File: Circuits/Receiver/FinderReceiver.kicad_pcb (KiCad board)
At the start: 2 copper layers, 59 x 28 mm, 9 parts, among them P1 WRITER-VCC, SW1 SW_PUSH, U1 TWE_LITE_SMD, U2 NJU72501MJE

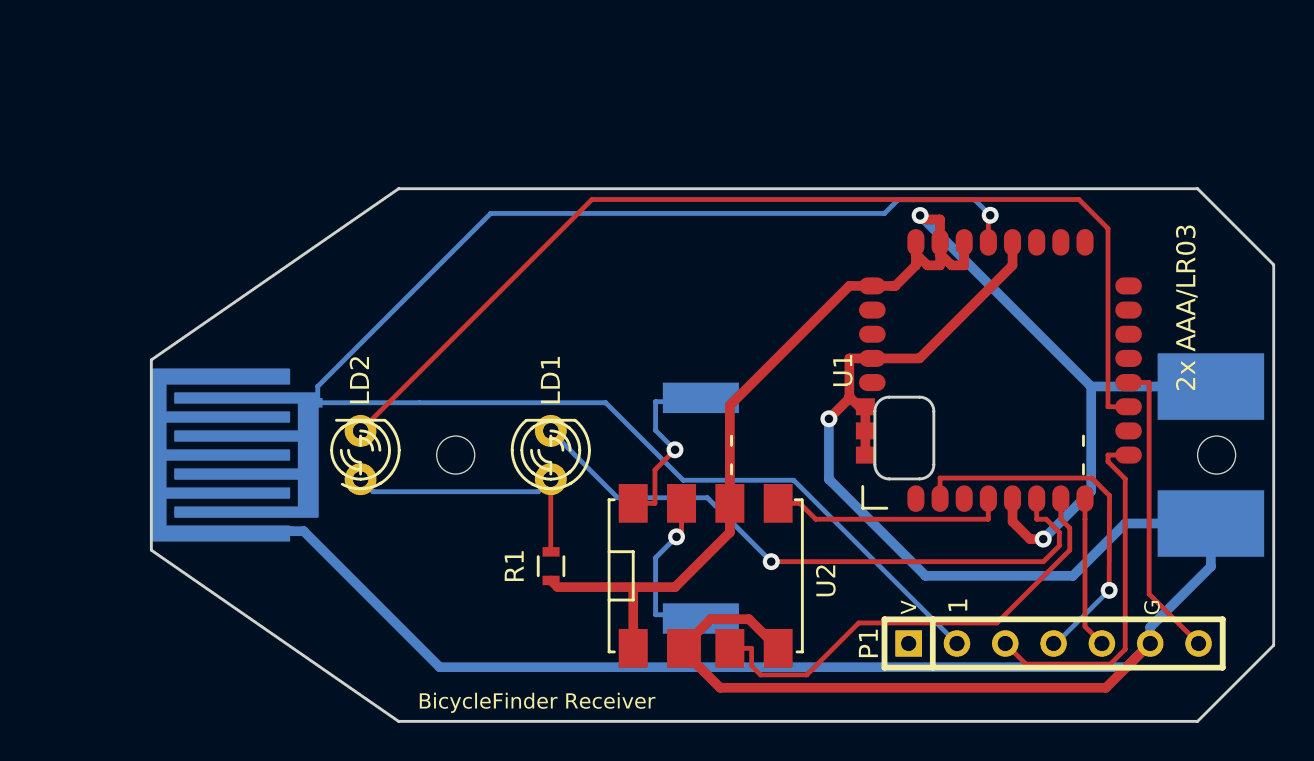
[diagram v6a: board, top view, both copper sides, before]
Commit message: Relocated all parts.
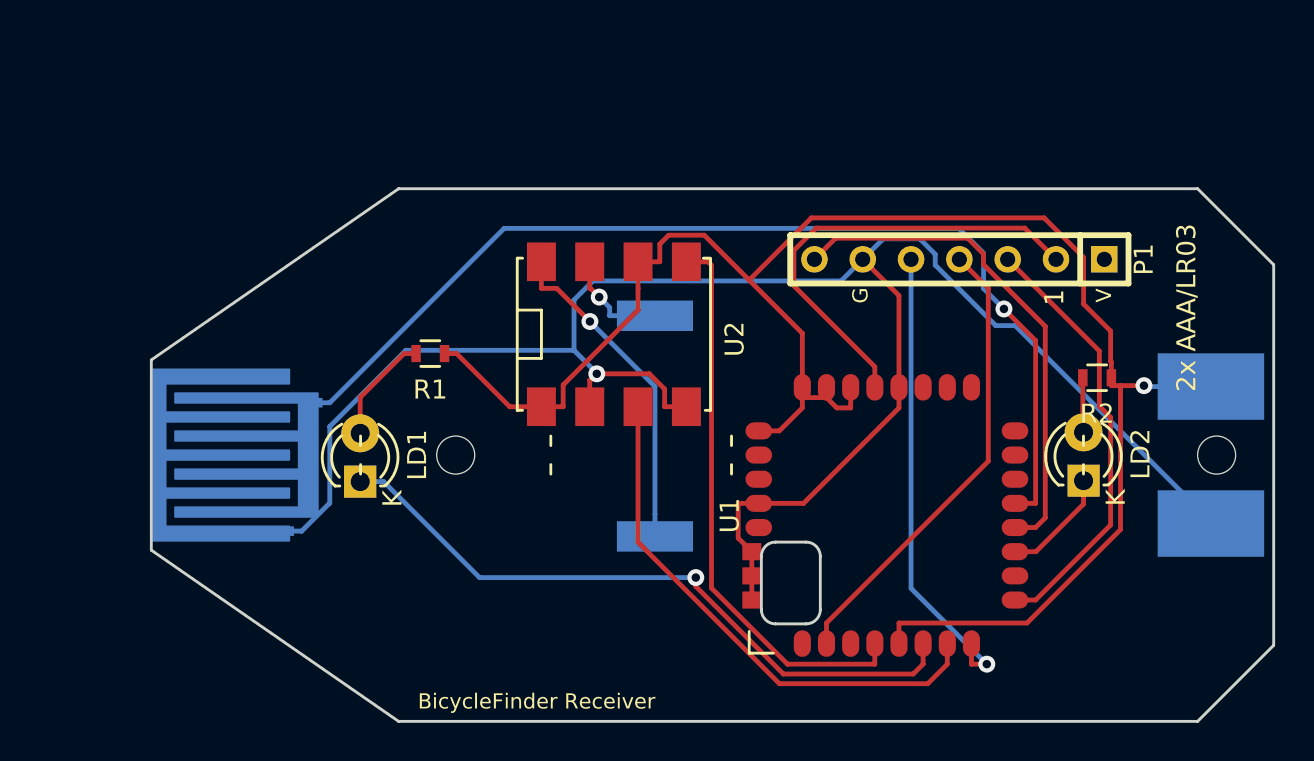
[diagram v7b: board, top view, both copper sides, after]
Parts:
- added R2: 680, Resistors_SMD:R_0603, F.Cu at (69.6, 33.8)
- LD2: footprint favorites:LED-3MM -> LEDs:LED-3MM
- moved LD2 38.0 mm to (68.9, 39.2)
- moved P1 20.8 mm to (62.4, 27.6), turned to 180 degrees
- moved U2 13.6 mm to (44.2, 31.5)
- moved R1 12.9 mm to (34.5, 32.5), turned to 180 degrees
- moved LD1 10.1 mm to (30.9, 39.2)
- moved U1 9.68 mm to (58.5, 41.0)
- moved SP1 4.95 mm to (46.4, 36.3), turned to 90 degrees
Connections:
- LD1 pad 1: /LED -> /DO3
- LD1 pad 2: /DO3 -> /LED1
- LD2 pad 1: /LED -> /DO4
- LD2 pad 2: /DO4 -> /LED2
- R1 pad 2: /LED -> /LED1
- SW1 pad 1: /RST -> /DI1
- U1 pad 13: Net-(U1-Pad13) -> /DI1
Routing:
- net /RST: track 80.9 -> 23.9 mm, vias 1 -> 0
- net /DI1: track 0.00 -> 54.7 mm, vias 0 -> 1
- net /DO4: track 55.4 -> 5.87 mm
- net GND: track 134.8 -> 99.4 mm
- net VCC: track 73.7 -> 94.4 mm, vias 2 -> 1
- net /EN2: track 12.5 -> 29.7 mm
- net /TXD: track 7.98 -> 24.8 mm, vias 0 -> 1
- net /LED: track 14.4 -> 0.00 mm
- net /CFG: track 15.9 -> 26.7 mm
- net /VO1: track 9.73 -> 17.4 mm
- net /LED1: track 0.00 -> 5.78 mm
- net /PRG: track 19.4 -> 24.3 mm, vias 1 -> 0
- net /RXD: track 18.7 -> 22.9 mm
- net /SOUND: track 24.6 -> 28.0 mm
- net /VO2: track 8.80 -> 5.67 mm
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
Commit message: Relocated base PCB.
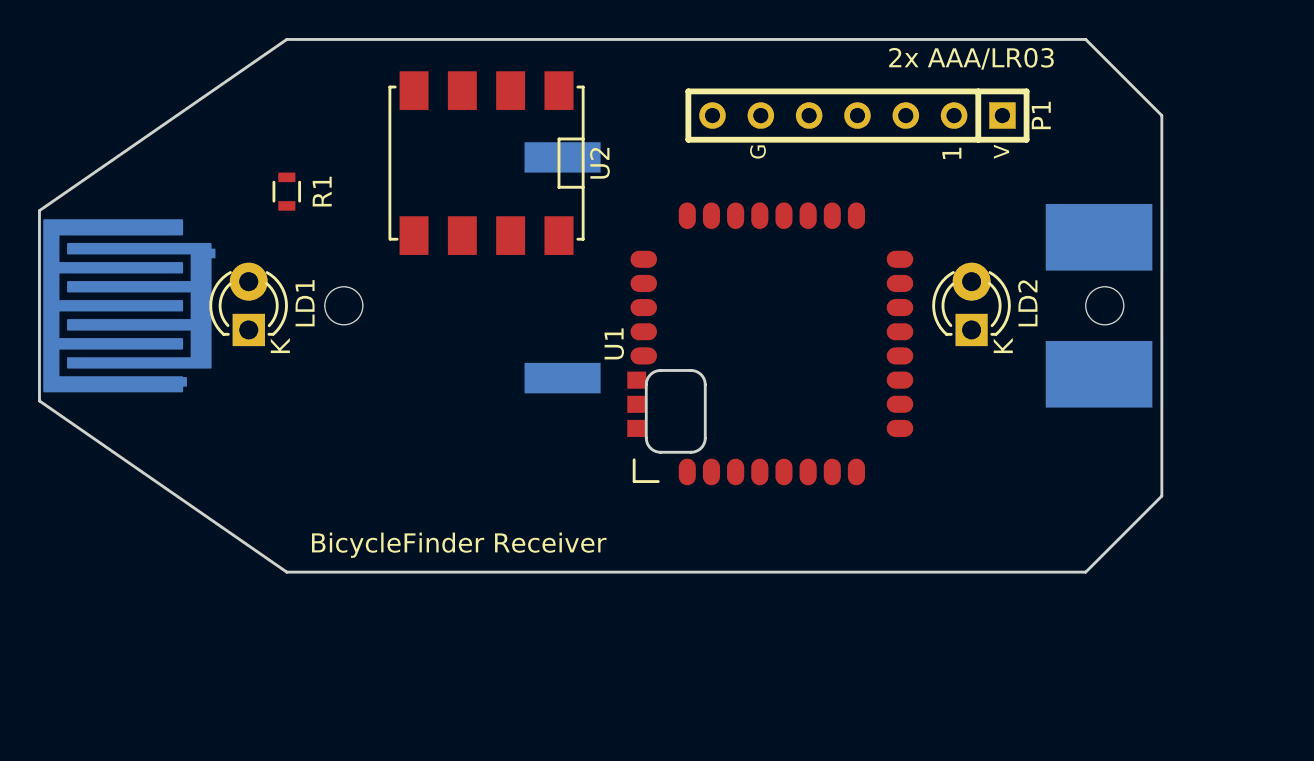
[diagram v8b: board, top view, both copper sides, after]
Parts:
- removed R2: 680, Resistors_SMD:R_0603
- moved R1 11.4 mm to (27.0, 24.0), turned to 270 degrees
- moved U2 11.2 mm to (37.5, 22.5), turned to 180 degrees
- moved U1 10.9 mm to (52.5, 32.0)
- moved LD1 9.90 mm to (25.0, 31.3)
- moved LD2 9.87 mm to (63.0, 31.3)
- moved BT1 9.80 mm to (50.0, 30.0)
- moved SW1 9.66 mm to (18.5, 30.0)
- moved SP1 9.63 mm to (41.5, 28.0), turned to 270 degrees
- moved P1 9.26 mm to (57.0, 20.0)
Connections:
- LD1 pad 2: /LED1 -> /LED
- LD2 pad 2: /LED2 -> /LED
- R1 pad 2: /LED1 -> /LED
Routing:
- net GND: track 99.4 -> 0.00 mm, vias 1 -> 0
- net VCC: track 94.4 -> 0.00 mm, vias 1 -> 0
- net /DI1: track 54.7 -> 0.00 mm, vias 1 -> 0
- net /DO3: track 35.3 -> 0.00 mm, vias 1 -> 0
- net /EN2: track 29.7 -> 0.00 mm
- net /SOUND: track 28.0 -> 0.00 mm
- net /CFG: track 26.7 -> 0.00 mm
- net /TXD: track 24.8 -> 0.00 mm, vias 1 -> 0
- net /PRG: track 24.3 -> 0.00 mm
- net /RST: track 23.9 -> 0.00 mm
- net /RXD: track 22.9 -> 0.00 mm
- net /VO1: track 17.4 -> 0.00 mm, vias 1 -> 0
- net /DO4: track 5.87 -> 0.00 mm
- net /LED1: track 5.78 -> 0.00 mm
- net /VO2: track 5.67 -> 0.00 mm, vias 1 -> 0
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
